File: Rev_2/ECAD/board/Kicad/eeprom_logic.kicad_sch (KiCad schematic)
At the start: 5 parts, among them U10 4076B, U6 AT28C64B-15PU, U7 4076B, U8 4076B, U9 4076B

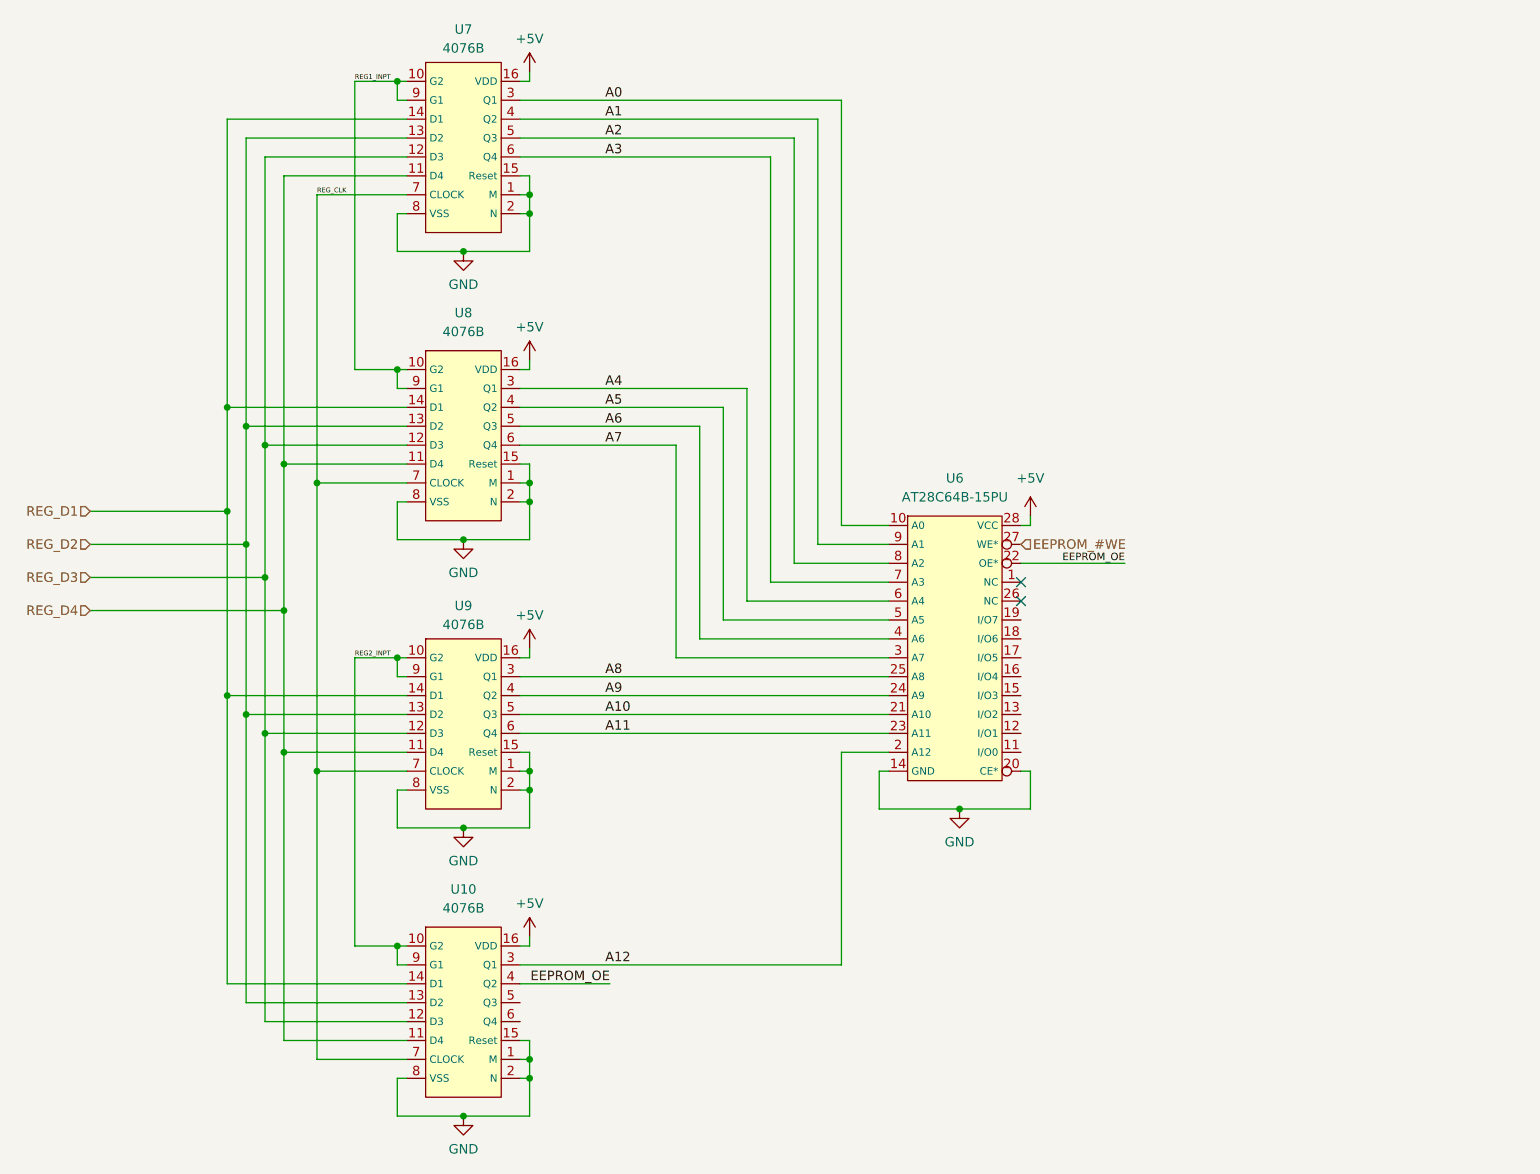
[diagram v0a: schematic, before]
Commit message: Added a sheet page for EEPROM_LOGIC
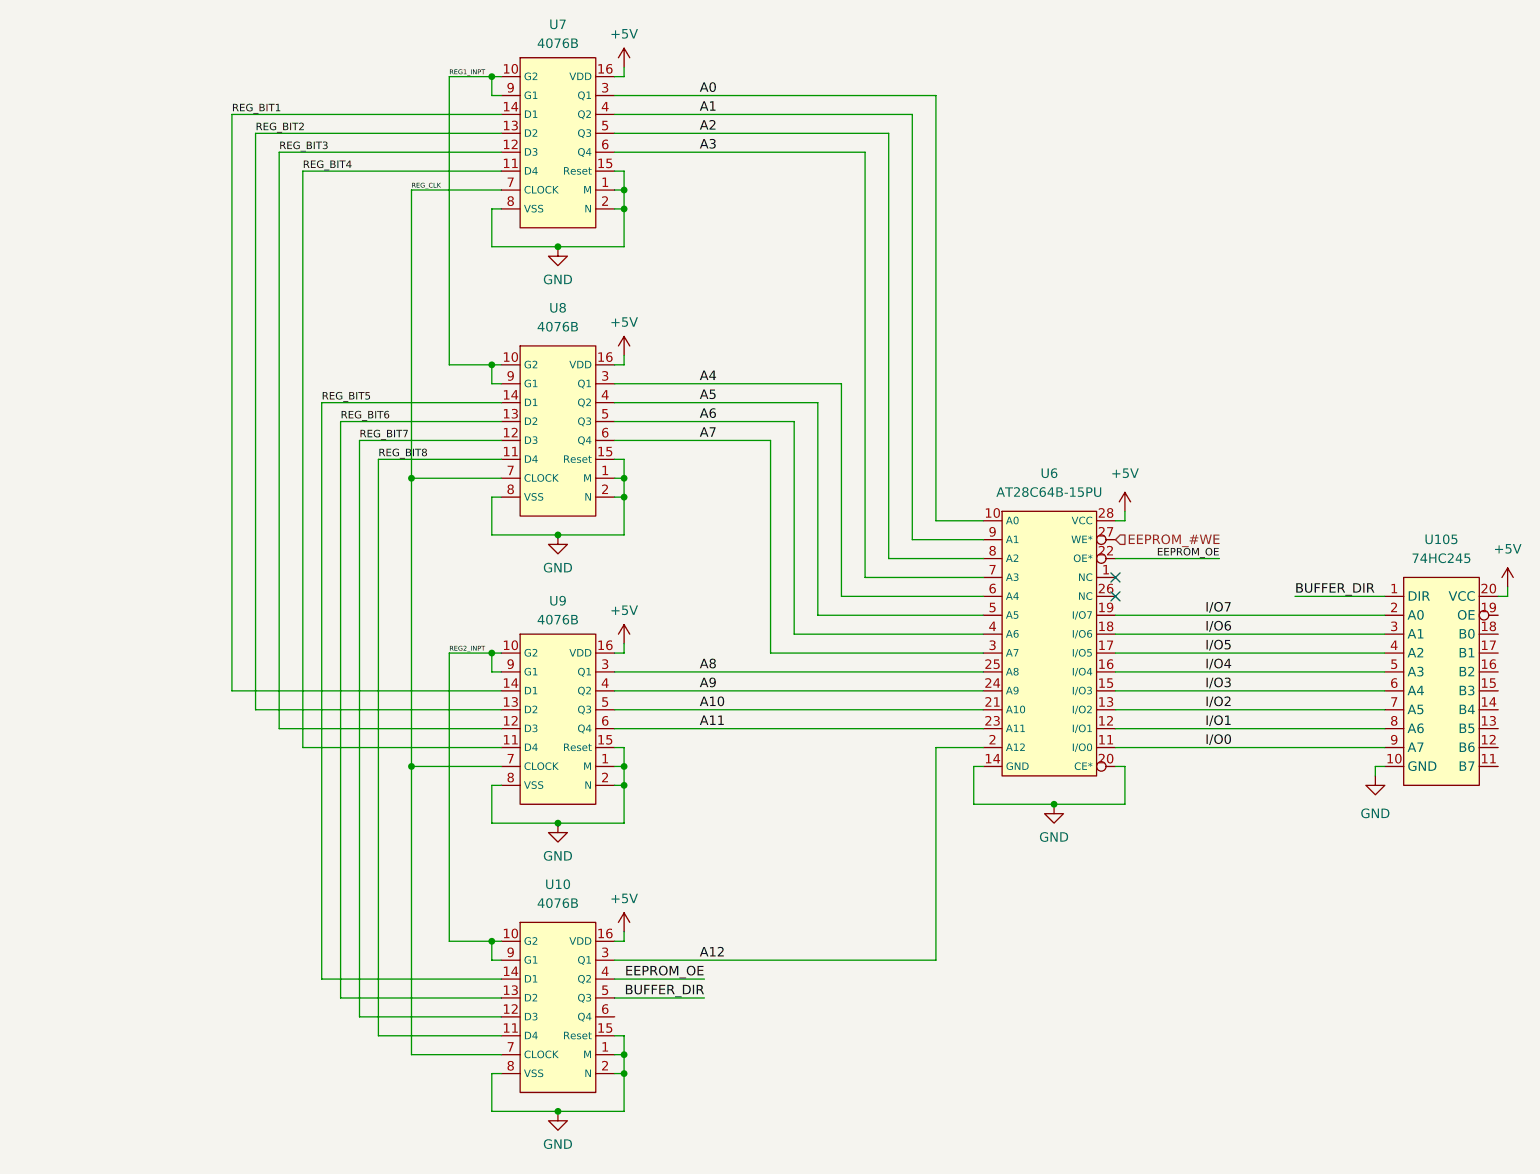
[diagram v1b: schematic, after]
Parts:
- added U105: 74HC245, EEPROM_PROGRAMMER:74HC245, symbol EEPROM_PROGRAMMER:74HC245
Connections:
- net +5V: now also U105.20 (VCC)
- net GND: now also U105.10 (GND)
- net I/O0: now reaches U6.11 (I/O0)
- net I/O0: now also U105.9 (A7)
- net I/O1: now reaches U6.12 (I/O1)
- net I/O1: now also U105.8 (A6)
- net I/O2: now reaches U6.13 (I/O2)
- net I/O2: now also U105.7 (A5)
- net I/O3: now reaches U6.15 (I/O3)
- net I/O3: now also U105.6 (A4)
- net I/O4: now reaches U6.16 (I/O4)
- net I/O4: now also U105.5 (A3)
- net I/O5: now reaches U6.17 (I/O5)
- net I/O5: now also U105.4 (A2)
- net I/O6: now reaches U6.18 (I/O6)
- net I/O6: now also U105.3 (A1)
- net I/O7: now reaches U6.19 (I/O7)
- net I/O7: now also U105.2 (A0)
- net BUFFER_DIR: now reaches U10.5 (Q3)
- net BUFFER_DIR: now also U105.1 (DIR)
- net REG_D1 renamed REG_BIT1
- net REG_BIT1: no longer U10.14 (D1), U8.14 (D1)
- net REG_D2 renamed REG_BIT2
- net REG_BIT2: no longer U10.13 (D2), U8.13 (D2)
- net REG_D3 renamed REG_BIT3
- net REG_BIT3: no longer U10.12 (D3), U8.12 (D3)
- net REG_D4 renamed REG_BIT4
- net REG_BIT4: no longer U10.11 (D4), U8.11 (D4)
- new net REG_BIT5: U10.14 (D1), U8.14 (D1)
- new net REG_BIT6: U10.13 (D2), U8.13 (D2)
- new net REG_BIT7: U10.12 (D3), U8.12 (D3)
- new net REG_BIT8: U10.11 (D4), U8.11 (D4)
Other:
- moved on the sheet: U10, U6, U7, U8, U9

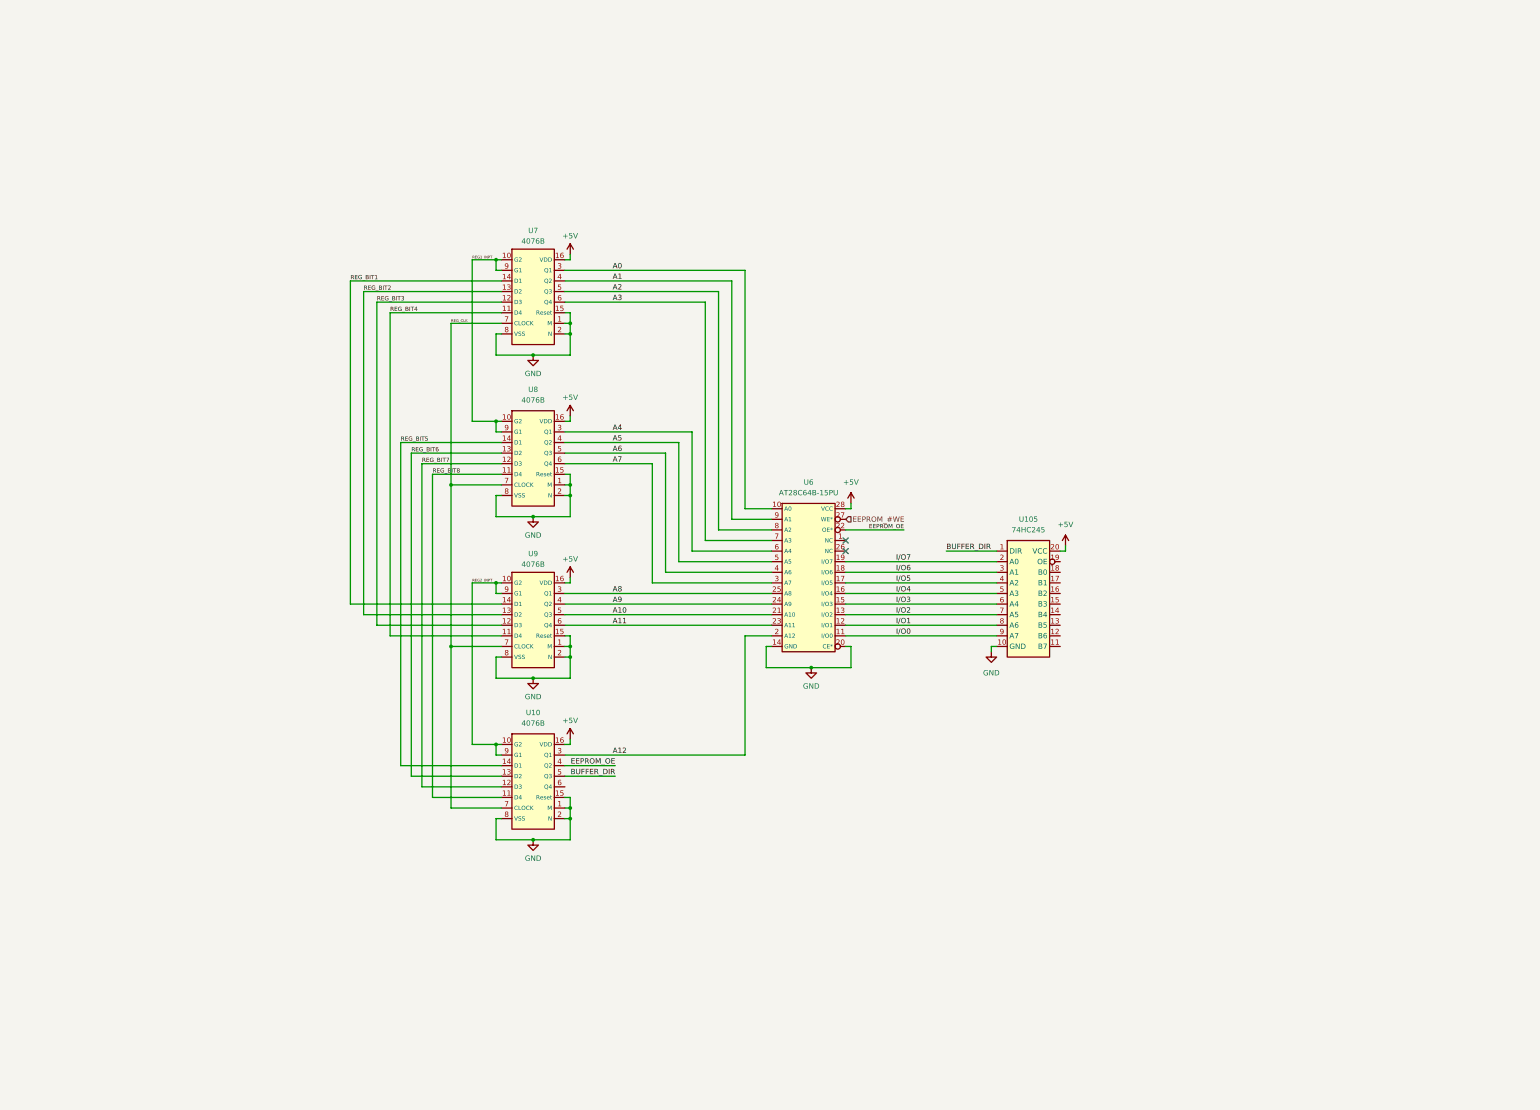
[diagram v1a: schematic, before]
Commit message: Finished most of EEPROM LOGIC
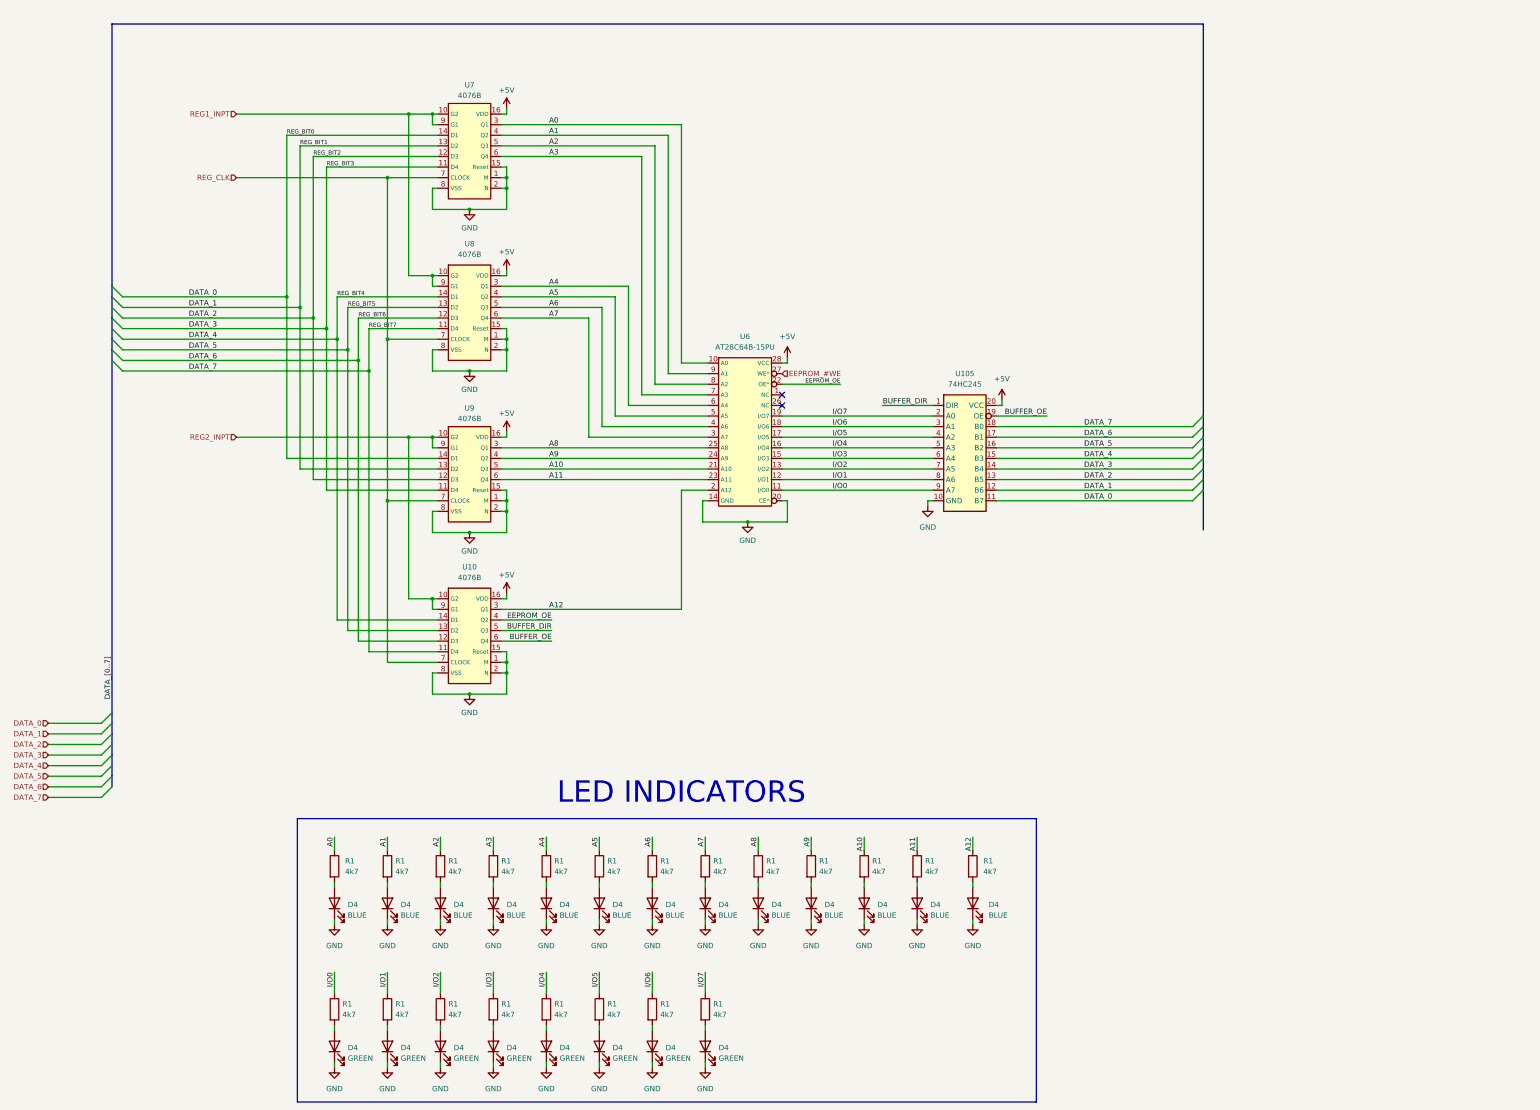
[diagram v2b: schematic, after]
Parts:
- added D4 (x8): GREEN, LED_SMD:LED_0805_2012Metric_Pad1.15x1.40mm_HandSolder, symbol Device:LED
- added D4 (x13): BLUE, LED_SMD:LED_0805_2012Metric_Pad1.15x1.40mm_HandSolder, symbol Device:LED
- added R1 (x21): 4k7, Resistor_SMD:R_0805_2012Metric_Pad1.20x1.40mm_HandSolder, symbol Device:R
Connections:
- net REG_BIT1 is gone; now on net DATA_0: U7.14 (D1), U9.14 (D1)
- net REG_BIT2 is gone; now on net DATA_1: U7.13 (D2), U9.13 (D2)
- net REG_BIT3 is gone; now on net DATA_2: U7.12 (D3), U9.12 (D3)
- net REG_BIT4 is gone; now on net DATA_3: U7.11 (D4), U9.11 (D4)
- net REG_BIT5 is gone; now on net DATA_4: U10.14 (D1), U8.14 (D1)
- net REG_BIT6 is gone; now on net DATA_5: U10.13 (D2), U8.13 (D2)
- net REG_BIT7 is gone; now on net DATA_6: U10.12 (D3), U8.12 (D3)
- net REG_BIT8 is gone; now on net DATA_7: U10.11 (D4), U8.11 (D4)
- net A0: now also R1.1
- net A1: now also R1.1
- net A10: now also R1.1
- net A11: now also R1.1
- net A12: now also R1.1
- net A2: now also R1.1
- net A3: now also R1.1
- net A4: now also R1.1
- net A5: now also R1.1
- net A6: now also R1.1
- net A7: now also R1.1
- net A8: now also R1.1
- net A9: now also R1.1
- net GND: now also D4.1 (K), D4.1 (K), D4.1 (K), D4.1 (K), D4.1 (K), D4.1 (K), D4.1 (K), D4.1 (K), D4.1 (K), D4.1 (K), D4.1 (K), D4.1 (K), D4.1 (K), D4.1 (K), D4.1 (K), D4.1 (K), D4.1 (K), D4.1 (K), D4.1 (K), D4.1 (K), D4.1 (K)
- net I/O0: now also R1.1
- net I/O1: now also R1.1
- net I/O2: now also R1.1
- net I/O3: now also R1.1
- net I/O4: now also R1.1
- net I/O5: now also R1.1
- net I/O6: now also R1.1
- net I/O7: now also R1.1
- net BUFFER_OE: now reaches U10.6 (Q4)
- net BUFFER_OE: now also U105.19 (OE)
- net DATA_0: now reaches U105.11 (B7)
- net DATA_1: now reaches U105.12 (B6)
- net DATA_2: now reaches U105.13 (B5)
- net DATA_3: now reaches U105.14 (B4)
- net DATA_4: now reaches U105.15 (B3)
- net DATA_5: now reaches U105.16 (B2)
- net DATA_6: now reaches U105.17 (B1)
- net DATA_7: now reaches U105.18 (B0)
- new net: D4.2 (A), R1.2 (x21)
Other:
- note added: "LED INDICATORS"
- moved on the sheet: U10, U105, U6, U7, U8, U9

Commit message: Added Bypass capacitors aswell as pullup resistors
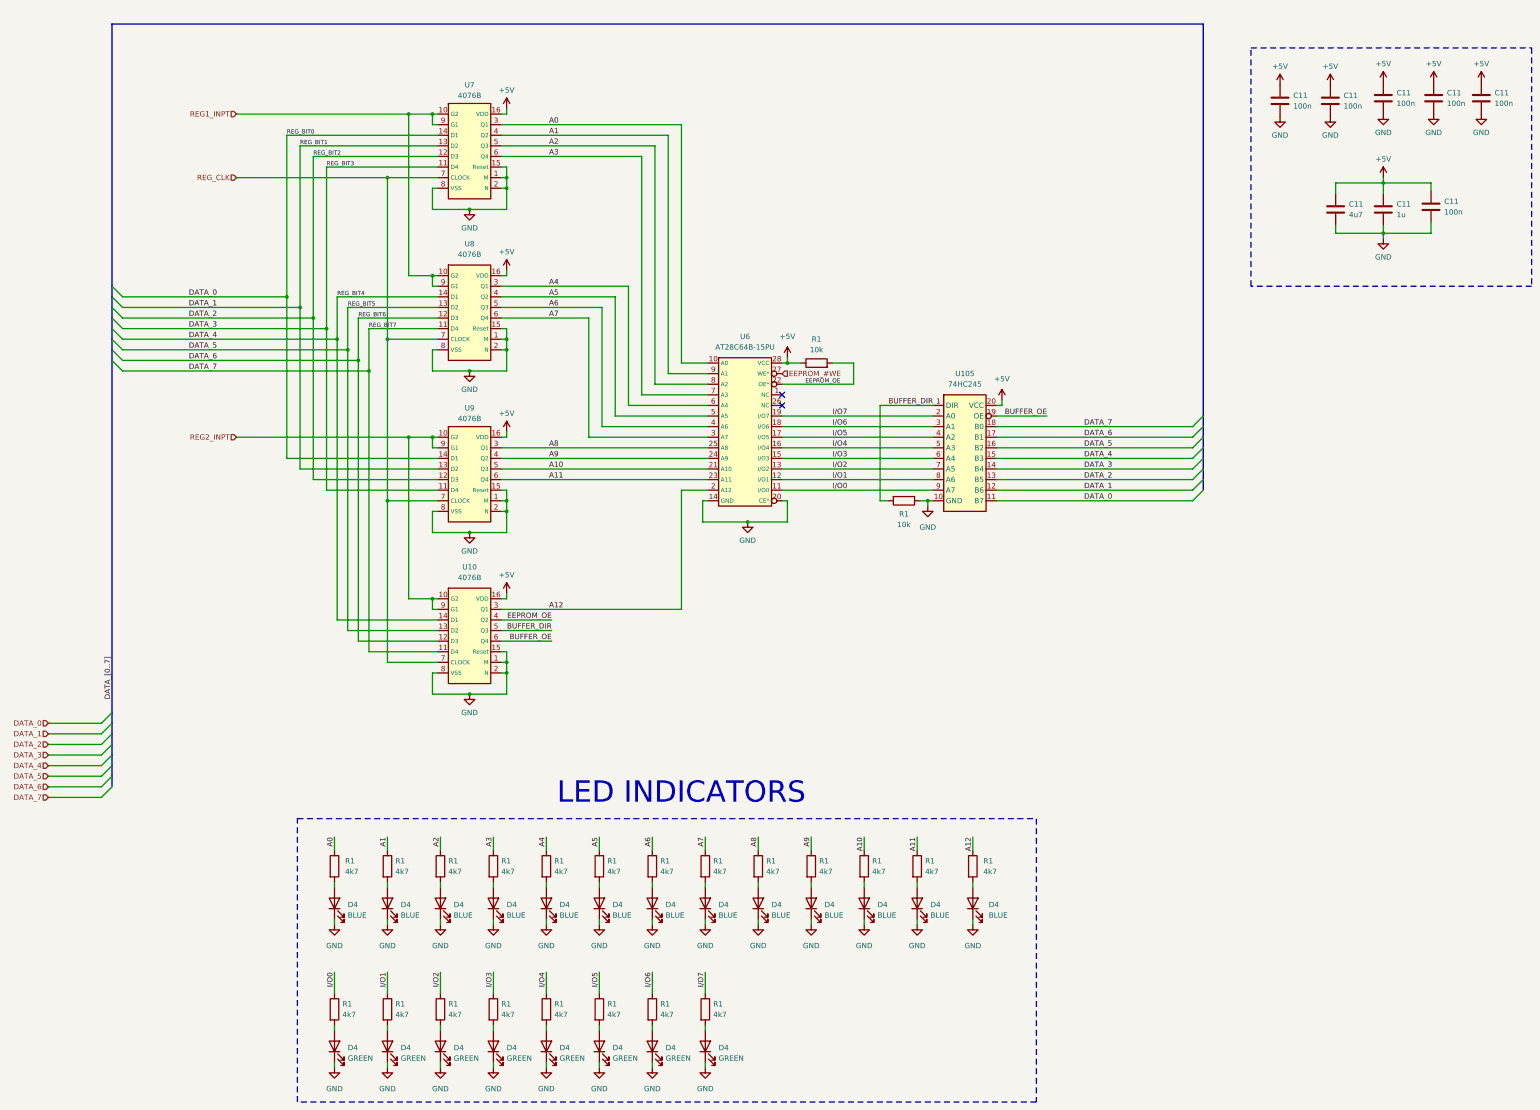
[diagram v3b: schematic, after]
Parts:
- added C11 (x6): 100n, Capacitor_THT:CP_Radial_D6.3mm_P2.50mm, symbol Device:C
- added C11: 4u7, Capacitor_THT:CP_Radial_D6.3mm_P2.50mm, symbol Device:C
- added C11: 1u, Capacitor_THT:CP_Radial_D6.3mm_P2.50mm, symbol Device:C
- added R1 (x2): 10k, Resistor_SMD:R_0805_2012Metric_Pad1.20x1.40mm_HandSolder, symbol Device:R
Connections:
- net +5V: now also C11.1, C11.1, C11.1, C11.1, C11.1, C11.1, C11.1, C11.1, R1.1
- net BUFFER_DIR: now also R1.2
- net EEPROM_OE: now also R1.2
- net GND: now also C11.2, C11.2, C11.2, C11.2, C11.2, C11.2, C11.2, C11.2, R1.1
